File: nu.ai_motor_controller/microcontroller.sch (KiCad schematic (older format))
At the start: 2 parts

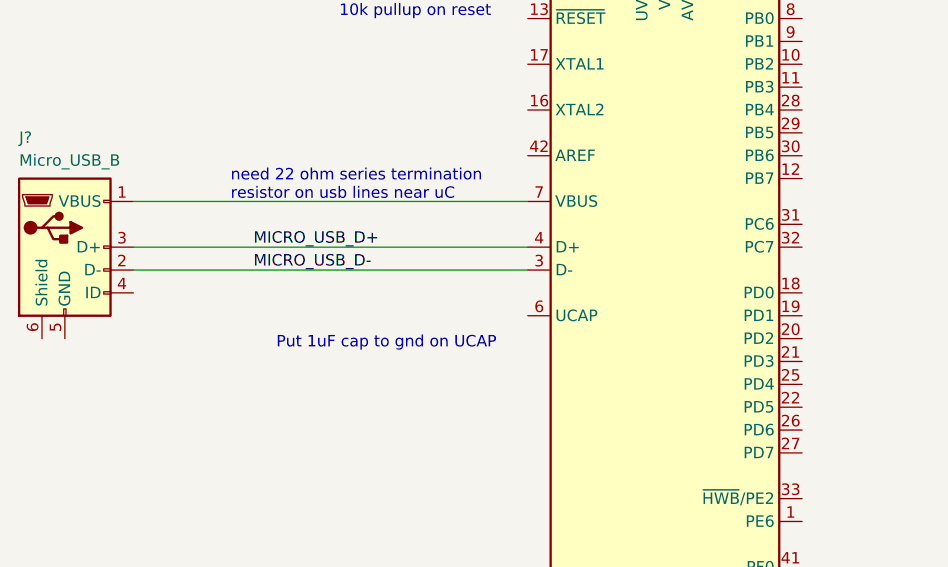
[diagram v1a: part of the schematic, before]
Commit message: Added termination resistors
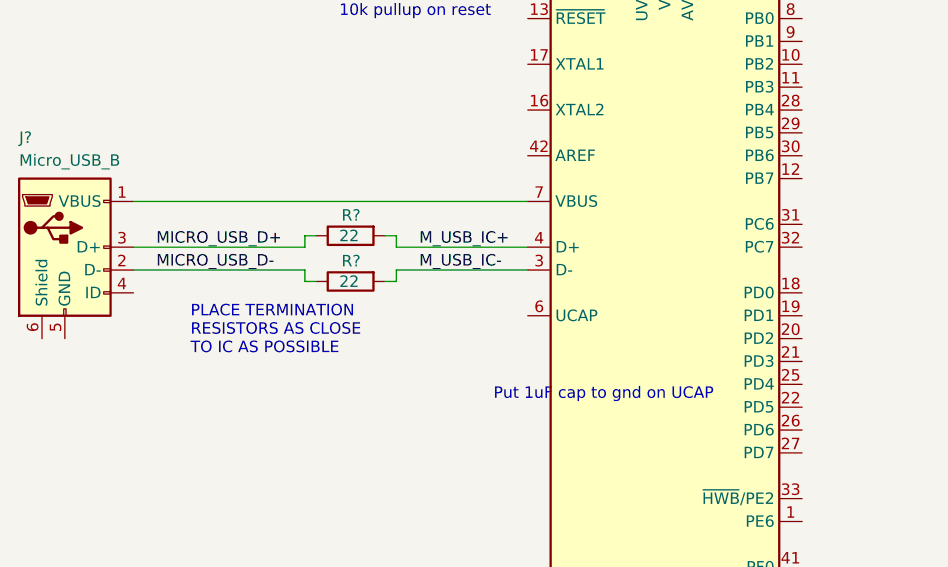
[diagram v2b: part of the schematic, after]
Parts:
- added R? (x2): RMCF0603FT22R0, 0603, symbol custom:RMCF0603FT22R0
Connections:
- net MICRO_USB_D+: now also R?.2; no longer U?.4 (D+)
- net MICRO_USB_D-: now also R?.2; no longer U?.3 (D-)
- new net M_USB_IC+: R?.1, U?.4 (D+)
- new net M_USB_IC-: R?.1, U?.3 (D-)
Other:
- note added: "PLACE TERMINATION\nRESISTORS AS CLOSE\nTO IC AS POSSIBLE"
- note removed: "need 22 ohm series termination\nresistor on usb lines near uC"
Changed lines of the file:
@@
 	1    0    0    -1
 $EndComp
-Wire Wire Line
-	3000 3225 4725 3225
-Wire Wire Line
-	4725 3325 3000 3325
-Text Label 3525 3225 0    50   ~ 0
+Text Label 3100 3225 0    50   ~ 0
 MICRO_USB_D+
-Text Label 3525 3325 0    50   ~ 0
+Text Label 3100 3325 0    50   ~ 0
 MICRO_USB_D-
-Text Notes 3425 3025 0    50   ~ 0
-need 22 ohm series termination\nresistor on usb lines near uC
+Text Notes 3250 3700 0    50   ~ 0
+PLACE TERMINATION\nRESISTORS AS CLOSE\nTO IC AS POSSIBLE
 Wire Wire Line
 	3000 3025 4725 3025
-Text Notes 3625 3675 0    50   ~ 0
+Text Notes 4575 3900 0    50   ~ 0
 Put 1uF cap to gnd on UCAP
 Text Notes 3900 2225 0    50   ~ 0
@@
 Text Notes 5475 1850 0    50   ~ 0
 Connect AVCC to VCC\nthrough a low pass filter
+$Comp
+L custom:RMCF0603FT22R0 R?
+U 1 1 5C4048F8
+P 3950 3375
+F 0 "R?" V 3890 3335 50  0000 L BNN
+F 1 "RMCF0603FT22R0" V 4075 3050 50  0001 L BNN
+F 2 "0603" V 4150 3275 50  0001 L BNN
+F 3 "~/datasheets/SEI-RMCF_RMCP.pdf" V 4250 3425 50  0001 C CNN
+F 4 "22" V 3980 3325 50  0000 L BNN "Resistance"
+	1    3950 3375
+	0    1    1    0
+$EndComp
+$Comp
+L custom:RMCF0603FT22R0 R?
+U 1 1 5C404A44
+P 3950 3175
+F 0 "R?" V 3890 3135 50  0000 L BNN
+F 1 "RMCF0603FT22R0" V 4075 2850 50  0001 L BNN
+F 2 "0603" V 4150 3075 50  0001 L BNN
+F 3 "~/datasheets/SEI-RMCF_RMCP.pdf" V 4250 3225 50  0001 C CNN
+F 4 "22" V 3980 3125 50  0000 L BNN "Resistance"
+	1    3950 3175
+	0    1    1    0
+$EndComp
+Wire Wire Line
+	4100 3175 4150 3175
+Wire Wire Line
+	4150 3175 4150 3225
+Wire Wire Line
+	4150 3225 4725 3225
+Wire Wire Line
+	4725 3325 4150 3325
+Wire Wire Line
+	4150 3325 4150 3375
+Wire Wire Line
+	4150 3375 4100 3375
+Wire Wire Line
+	3800 3375 3750 3375
+Wire Wire Line
+	3750 3325 3000 3325
+Wire Wire Line
+	3750 3325 3750 3375
+Wire Wire Line
+	3000 3225 3750 3225
+Wire Wire Line
+	3750 3225 3750 3175
+Wire Wire Line
+	3750 3175 3800 3175
+Text Label 4250 3225 0    50   ~ 0
+M_USB_IC+
+Text Label 4250 3325 0    50   ~ 0
+M_USB_IC-
 $EndSCHEMATC

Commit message: automated commit
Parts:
- added C?: CL10B105KA8NNNC, Capacitor_SMD:C_0603_1608Metric, symbol custom:CL10B105KA8NNNC
- added R?: CR0603-JW-103ELF, 0603, symbol custom:CR0603-JW-103ELF
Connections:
- net labels added: GND
- wire segments 13 -> 19
- no-connect marks 0 -> 1
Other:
- note added: "connect to power\n"
- note removed: "10k pullup on reset"
- note removed: "Put 1uF cap to gnd on UCAP"
- moved on the sheet: J?, R?, U?
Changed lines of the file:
@@
 L MCU_Microchip_ATmega:ATmega32U4-AU U?
 U 1 1 5C3ED06E
-P 5325 3725
-F 0 "U?" H 4825 5475 50  0000 L BNN
-F 1 "ATmega32U4-AU" H 5425 1975 50  0000 L TNN
-F 2 "Package_QFP:TQFP-44_10x10mm_P0.8mm" H 5325 3725 50  0001 C CIN
-F 3 "http://ww1.microchip.com/downloads/en/DeviceDoc/Atmel-7766-8-bit-AVR-ATmega16U4-32U4_Datasheet.pdf" H 5325 3725 50  0001 C CNN
-	1    5325 3725
+P 5350 3700
+F 0 "U?" H 4850 5450 50  0000 L BNN
+F 1 "ATmega32U4-AU" H 5450 1950 50  0000 L TNN
+F 2 "Package_QFP:TQFP-44_10x10mm_P0.8mm" H 5350 3700 50  0001 C CIN
+F 3 "http://ww1.microchip.com/downloads/en/DeviceDoc/Atmel-7766-8-bit-AVR-ATmega16U4-32U4_Datasheet.pdf" H 5350 3700 50  0001 C CNN
+	1    5350 3700
 	1    0    0    -1
 $EndComp
@@
 L custom:DX4R105JJCR1800 J?
 U 1 1 5C3ED2E2
-P 2700 3225
-F 0 "J?" H 2500 3675 50  0000 L BNN
-F 1 "DX4R105JJCR1800" H 2400 2425 50  0001 L BNN
-F 2 "" H 2850 3175 50  0001 C CNN
-F 3 "SJ113218.pdf" H 2850 3175 50  0001 L BNN
-F 4 "Micro_USB_B" H 2500 3575 50  0000 L BNN "Description"
-	1    2700 3225
+P 2000 3200
+F 0 "J?" H 1800 3650 50  0000 L BNN
+F 1 "DX4R105JJCR1800" H 1700 2400 50  0001 L BNN
+F 2 "" H 2150 3150 50  0001 C CNN
+F 3 "SJ113218.pdf" H 2150 3150 50  0001 L BNN
+F 4 "Micro_USB_B" H 1800 3550 50  0000 L BNN "Description"
+	1    2000 3200
 	1    0    0    -1
 $EndComp
-Text Label 3100 3225 0    50   ~ 0
+Text Label 3050 3200 0    50   ~ 0
 MICRO_USB_D+
-Text Label 3100 3325 0    50   ~ 0
+Text Label 3050 3300 0    50   ~ 0
 MICRO_USB_D-
-Text Notes 3250 3700 0    50   ~ 0
+Text Notes 3225 3675 0    50   ~ 0
 PLACE TERMINATION\nRESISTORS AS CLOSE\nTO IC AS POSSIBLE
 Wire Wire Line
-	3000 3025 4725 3025
-Text Notes 4575 3900 0    50   ~ 0
-Put 1uF cap to gnd on UCAP
-Text Notes 3900 2225 0    50   ~ 0
-10k pullup on reset
+	2300 3000 4750 3000
 Text Notes 5475 1850 0    50   ~ 0
 Connect AVCC to VCC\nthrough a low pass filter
@@
 L custom:RMCF0603FT22R0 R?
 U 1 1 5C4048F8
-P 3950 3375
-F 0 "R?" V 3890 3335 50  0000 L BNN
-F 1 "RMCF0603FT22R0" V 4075 3050 50  0001 L BNN
-F 2 "0603" V 4150 3275 50  0001 L BNN
-F 3 "~/datasheets/SEI-RMCF_RMCP.pdf" V 4250 3425 50  0001 C CNN
-F 4 "22" V 3980 3325 50  0000 L BNN "Resistance"
-	1    3950 3375
+P 3900 3350
+F 0 "R?" V 3840 3310 50  0000 L BNN
+F 1 "RMCF0603FT22R0" V 4025 3025 50  0001 L BNN
+F 2 "0603" V 4100 3250 50  0001 L BNN
+F 3 "~/datasheets/SEI-RMCF_RMCP.pdf" V 4200 3400 50  0001 C CNN
+F 4 "22" V 3930 3300 50  0000 L BNN "Resistance"
+	1    3900 3350
 	0    1    1    0
 $EndComp
@@
 L custom:RMCF0603FT22R0 R?
 U 1 1 5C404A44
-P 3950 3175
-F 0 "R?" V 3890 3135 50  0000 L BNN
-F 1 "RMCF0603FT22R0" V 4075 2850 50  0001 L BNN
-F 2 "0603" V 4150 3075 50  0001 L BNN
-F 3 "~/datasheets/SEI-RMCF_RMCP.pdf" V 4250 3225 50  0001 C CNN
-F 4 "22" V 3980 3125 50  0000 L BNN "Resistance"
-	1    3950 3175
+P 3900 3150
+F 0 "R?" V 3840 3110 50  0000 L BNN
+F 1 "RMCF0603FT22R0" V 4025 2825 50  0001 L BNN
+F 2 "0603" V 4100 3050 50  0001 L BNN
+F 3 "~/datasheets/SEI-RMCF_RMCP.pdf" V 4200 3200 50  0001 C CNN
+F 4 "22" V 3930 3100 50  0000 L BNN "Resistance"
+	1    3900 3150
 	0    1    1    0
 $EndComp
 Wire Wire Line
-	4100 3175 4150 3175
+	4050 3150 4100 3150
 Wire Wire Line
-	4150 3175 4150 3225
+	4100 3150 4100 3200
 Wire Wire Line
-	4150 3225 4725 3225
+	4100 3300 4100 3350
 Wire Wire Line
-	4725 3325 4150 3325
+	4100 3350 4050 3350
 Wire Wire Line
-	4150 3325 4150 3375
+	3750 3350 3700 3350
 Wire Wire Line
-	4150 3375 4100 3375
+	3700 3300 2300 3300
 Wire Wire Line
-	3800 3375 3750 3375
+	3700 3300 3700 3350
 Wire Wire Line
-	3750 3325 3000 3325
+	2300 3200 3700 3200
 Wire Wire Line
-	3750 3325 3750 3375
+	3700 3200 3700 3150
 Wire Wire Line
-	3000 3225 3750 3225
+	3700 3150 3750 3150
+Text Label 4200 3200 0    50   ~ 0
+M_USB_IC+
+Text Label 4200 3300 0    50   ~ 0
+M_USB_IC-
+$Comp
+L custom:CL10B105KA8NNNC C?
+U 1 1 5C414E9B
+P 4650 3750
+F 0 "C?" H 4800 3850 50  0000 L BNN
+F 1 "CL10B105KA8NNNC" H 3700 3300 50  0001 L BNN
+F 2 "Capacitor_SMD:C_0603_1608Metric" H 3700 3200 50  0001 L BNN
+F 3 "datasheets/CL10B105KA8NNNC.pdf" H 3700 3100 50  0001 L BNN
+F 4 "1uF" H 4800 3750 50  0000 L BNN "Capacitance"
+F 5 "25V" H 4800 3650 50  0000 L BNN "Rating"
+	1    4650 3750
+	-1   0    0    -1
+$EndComp
+$Comp
+L power:GND #PWR?
+U 1 1 5C414F68
+P 4650 3950
+F 0 "#PWR?" H 4650 3700 50  0001 C CNN
+F 1 "GND" H 4650 3800 50  0000 C CNN
+F 2 "" H 4650 3950 50  0001 C CNN
+F 3 "" H 4650 3950 50  0001 C CNN
+	1    4650 3950
+	1    0    0    -1
+$EndComp
 Wire Wire Line
-	3750 3225 3750 3175
+	4650 3950 4650 3900
 Wire Wire Line
-	3750 3175 3800 3175
-Text Label 4250 3225 0    50   ~ 0
-M_USB_IC+
-Text Label 4250 3325 0    50   ~ 0
-M_USB_IC-
+	4650 3600 4650 3500
+Wire Wire Line
+	4650 3500 4750 3500
+Wire Wire Line
+	4100 3300 4750 3300
+Wire Wire Line
+	4100 3200 4750 3200
+$Comp
+L custom:CR0603-JW-103ELF R?
+U 1 1 5C41A4AA
+P 4650 1950
+F 0 "R?" V 4590 1910 50  0000 L BNN
+F 1 "CR0603-JW-103ELF" V 4775 1625 50  0001 L BNN
+F 2 "0603" V 4850 1850 50  0001 L BNN
+F 3 "~/datasheets/chpreztr.pdf" V 4950 1500 50  0001 L BNN
+F 4 "10k" V 4680 1880 50  0000 L BNN "Resistance"
+	1    4650 1950
+	1    0    0    -1
+$EndComp
+Wire Wire Line
+	4650 2100 4650 2200
+Wire Wire Line
+	4650 2200 4750 2200
+Wire Wire Line
+	4650 1800 4650 1700
+Text Notes 4300 1600 0    50   ~ 0
+connect to power\n
+NoConn ~ 2300 3400
 $EndSCHEMATC

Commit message: automated commit
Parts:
- added L?: CIS10P300AC, 0603, symbol custom:CIS10P300AC
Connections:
- net labels added: +5V
- wire segments 19 -> 25
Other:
- note removed: "Connect AVCC to VCC\nthrough a low pass filter"
- note removed: "connect to power\n"
- moved on the sheet: R?
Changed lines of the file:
@@
 Wire Wire Line
 	2300 3000 4750 3000
-Text Notes 5475 1850 0    50   ~ 0
-Connect AVCC to VCC\nthrough a low pass filter
 $Comp
 L custom:RMCF0603FT22R0 R?
@@
 L custom:CR0603-JW-103ELF R?
 U 1 1 5C41A4AA
-P 4650 1950
-F 0 "R?" V 4590 1910 50  0000 L BNN
-F 1 "CR0603-JW-103ELF" V 4775 1625 50  0001 L BNN
-F 2 "0603" V 4850 1850 50  0001 L BNN
-F 3 "~/datasheets/chpreztr.pdf" V 4950 1500 50  0001 L BNN
-F 4 "10k" V 4680 1880 50  0000 L BNN "Resistance"
-	1    4650 1950
+P 4650 1750
+F 0 "R?" V 4590 1710 50  0000 L BNN
+F 1 "CR0603-JW-103ELF" V 4775 1425 50  0001 L BNN
+F 2 "0603" V 4850 1650 50  0001 L BNN
+F 3 "~/datasheets/chpreztr.pdf" V 4950 1300 50  0001 L BNN
+F 4 "10k" V 4680 1680 50  0000 L BNN "Resistance"
+	1    4650 1750
 	1    0    0    -1
 $EndComp
 Wire Wire Line
-	4650 2100 4650 2200
+	4650 1900 4650 2200
 Wire Wire Line
 	4650 2200 4750 2200
+NoConn ~ 2300 3400
+$Comp
+L custom:CIS10P300AC L?
+U 1 1 5C41689A
+P 5450 1700
+F 0 "L?" H 5550 1700 50  0000 L BNN
+F 1 "CIS10P300AC" H 5550 1400 50  0001 L BNN
+F 2 "0603" H 5550 1500 50  0001 L BNN
+F 3 "~/datasheets/CIS10P300AC.pdf" H 5550 1300 50  0001 L BNN
+F 4 "30@100MHz" H 5550 1600 50  0000 L BNN "Impedance"
+	1    5450 1700
+	1    0    0    -1
+$EndComp
 Wire Wire Line
-	4650 1800 4650 1700
-Text Notes 4300 1600 0    50   ~ 0
-connect to power\n
-NoConn ~ 2300 3400
+	5450 1900 5450 1850
+$Comp
+L power:+5V #PWR?
+U 1 1 5C416CDF
+P 5350 1450
+F 0 "#PWR?" H 5350 1300 50  0001 C CNN
+F 1 "+5V" H 5350 1590 50  0000 C CNN
+F 2 "" H 5350 1450 50  0001 C CNN
+F 3 "" H 5350 1450 50  0001 C CNN
+	1    5350 1450
+	1    0    0    -1
+$EndComp
+$Comp
+L power:+5V #PWR?
+U 1 1 5C416CFF
+P 4650 1450
+F 0 "#PWR?" H 4650 1300 50  0001 C CNN
+F 1 "+5V" H 4650 1590 50  0000 C CNN
+F 2 "" H 4650 1450 50  0001 C CNN
+F 3 "" H 4650 1450 50  0001 C CNN
+	1    4650 1450
+	1    0    0    -1
+$EndComp
+Wire Wire Line
+	4650 1450 4650 1600
+Wire Wire Line
+	5350 1450 5350 1500
+Wire Wire Line
+	5450 1550 5450 1500
+Wire Wire Line
+	5450 1500 5350 1500
+Connection ~ 5350 1500
+Wire Wire Line
+	5350 1500 5350 1900
+$Comp
+L power:GND #PWR?
+U 1 1 5C417D83
+P 5350 5600
+F 0 "#PWR?" H 5350 5350 50  0001 C CNN
+F 1 "GND" H 5350 5450 50  0000 C CNN
+F 2 "" H 5350 5600 50  0001 C CNN
+F 3 "" H 5350 5600 50  0001 C CNN
+	1    5350 5600
+	1    0    0    -1
+$EndComp
+Wire Wire Line
+	5350 5600 5350 5500
 $EndSCHEMATC

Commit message: automated commit
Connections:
- net +5V: now also U?.2 (UVCC)
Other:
- note added: "put .5A resettable fuse on vbus\n"
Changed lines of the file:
@@
 	4650 1450 4650 1600
 Wire Wire Line
-	5350 1450 5350 1500
-Wire Wire Line
-	5450 1550 5450 1500
-Wire Wire Line
 	5450 1500 5350 1500
-Connection ~ 5350 1500
-Wire Wire Line
-	5350 1500 5350 1900
 $Comp
 L power:GND #PWR?
@@
 Wire Wire Line
 	5350 5600 5350 5500
+Wire Wire Line
+	5250 1900 5250 1800
+Wire Wire Line
+	5250 1800 5350 1800
+Connection ~ 5350 1800
+Wire Wire Line
+	5350 1800 5350 1900
+Wire Wire Line
+	5350 1500 5350 1800
+Connection ~ 5350 1500
+Wire Wire Line
+	5350 1450 5350 1500
+Wire Wire Line
+	5450 1550 5450 1500
+Text Notes 2900 2950 0    50   ~ 0
+put .5A resettable fuse on vbus\n
 $EndSCHEMATC

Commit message: automated commit
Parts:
- added C?: CL10B104KO8NNNC, Capacitor_SMD:C_0603_1608Metric, symbol custom:CL10B104KO8NNNC
- added C?: CL10B105KA8NNNC, Capacitor_SMD:C_0603_1608Metric, symbol custom:CL10B105KA8NNNC
- added L?: CIS10P300AC, 0603, symbol custom:CIS10P300AC
- added R?: RC0603JR-071KL, 0603, symbol custom:RC0603JR-071KL
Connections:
- net labels added: M_USB_D+, M_USB_D-, UGND, VBUS
- net labels removed: MICRO_USB_D+, MICRO_USB_D-
- wire segments 28 -> 47
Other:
- note added: "use CM1293A-04SO on data lines"
- moved on the sheet: J?, R?
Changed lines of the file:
@@
 L custom:DX4R105JJCR1800 J?
 U 1 1 5C3ED2E2
-P 2000 3200
-F 0 "J?" H 1800 3650 50  0000 L BNN
-F 1 "DX4R105JJCR1800" H 1700 2400 50  0001 L BNN
-F 2 "" H 2150 3150 50  0001 C CNN
-F 3 "SJ113218.pdf" H 2150 3150 50  0001 L BNN
-F 4 "Micro_USB_B" H 1800 3550 50  0000 L BNN "Description"
-	1    2000 3200
-	1    0    0    -1
-$EndComp
-Text Label 3050 3200 0    50   ~ 0
-MICRO_USB_D+
-Text Label 3050 3300 0    50   ~ 0
-MICRO_USB_D-
-Text Notes 3225 3675 0    50   ~ 0
+P 1550 1975
+F 0 "J?" H 1350 2425 50  0000 L BNN
+F 1 "DX4R105JJCR1800" H 1250 1175 50  0001 L BNN
+F 2 "" H 1700 1925 50  0001 C CNN
+F 3 "SJ113218.pdf" H 1700 1925 50  0001 L BNN
+F 4 "Micro_USB_B" H 1350 2325 50  0000 L BNN "Description"
+	1    1550 1975
+	1    0    0    -1
+$EndComp
+Text Label 1875 1975 0    50   ~ 0
+M_USB_D+
+Text Label 1875 2075 0    50   ~ 0
+M_USB_D-
+Text Notes 2250 2425 0    50   ~ 0
 PLACE TERMINATION\nRESISTORS AS CLOSE\nTO IC AS POSSIBLE
-Wire Wire Line
-	2300 3000 4750 3000
 $Comp
 L custom:RMCF0603FT22R0 R?
 U 1 1 5C4048F8
-P 3900 3350
-F 0 "R?" V 3840 3310 50  0000 L BNN
-F 1 "RMCF0603FT22R0" V 4025 3025 50  0001 L BNN
-F 2 "0603" V 4100 3250 50  0001 L BNN
-F 3 "~/datasheets/SEI-RMCF_RMCP.pdf" V 4200 3400 50  0001 C CNN
-F 4 "22" V 3930 3300 50  0000 L BNN "Resistance"
-	1    3900 3350
+P 2525 2125
+F 0 "R?" V 2465 2085 50  0000 L BNN
+F 1 "RMCF0603FT22R0" V 2650 1800 50  0001 L BNN
+F 2 "0603" V 2725 2025 50  0001 L BNN
+F 3 "~/datasheets/SEI-RMCF_RMCP.pdf" V 2825 2175 50  0001 C CNN
+F 4 "22" V 2555 2075 50  0000 L BNN "Resistance"
+	1    2525 2125
 	0    1    1    0
 $EndComp
@@
 L custom:RMCF0603FT22R0 R?
 U 1 1 5C404A44
-P 3900 3150
-F 0 "R?" V 3840 3110 50  0000 L BNN
-F 1 "RMCF0603FT22R0" V 4025 2825 50  0001 L BNN
-F 2 "0603" V 4100 3050 50  0001 L BNN
-F 3 "~/datasheets/SEI-RMCF_RMCP.pdf" V 4200 3200 50  0001 C CNN
-F 4 "22" V 3930 3100 50  0000 L BNN "Resistance"
-	1    3900 3150
+P 2525 1925
+F 0 "R?" V 2465 1885 50  0000 L BNN
+F 1 "RMCF0603FT22R0" V 2650 1600 50  0001 L BNN
+F 2 "0603" V 2725 1825 50  0001 L BNN
+F 3 "~/datasheets/SEI-RMCF_RMCP.pdf" V 2825 1975 50  0001 C CNN
+F 4 "22" V 2555 1875 50  0000 L BNN "Resistance"
+	1    2525 1925
 	0    1    1    0
 $EndComp
 Wire Wire Line
-	4050 3150 4100 3150
-Wire Wire Line
-	4100 3150 4100 3200
-Wire Wire Line
-	4100 3300 4100 3350
-Wire Wire Line
-	4100 3350 4050 3350
-Wire Wire Line
-	3750 3350 3700 3350
-Wire Wire Line
-	3700 3300 2300 3300
-Wire Wire Line
-	3700 3300 3700 3350
-Wire Wire Line
-	2300 3200 3700 3200
-Wire Wire Line
-	3700 3200 3700 3150
-Wire Wire Line
-	3700 3150 3750 3150
-Text Label 4200 3200 0    50   ~ 0
+	2675 1925 2725 1925
+Wire Wire Line
+	2725 1925 2725 1975
+Wire Wire Line
+	2725 2075 2725 2125
+Wire Wire Line
+	2725 2125 2675 2125
+Wire Wire Line
+	2375 2125 2325 2125
+Wire Wire Line
+	2325 2075 1850 2075
+Wire Wire Line
+	2325 2075 2325 2125
+Wire Wire Line
+	1850 1975 2325 1975
+Wire Wire Line
+	2325 1975 2325 1925
+Wire Wire Line
+	2325 1925 2375 1925
+Text Label 4275 3200 0    50   ~ 0
 M_USB_IC+
-Text Label 4200 3300 0    50   ~ 0
+Text Label 4275 3300 0    50   ~ 0
 M_USB_IC-
 $Comp
@@
 U 1 1 5C414E9B
 P 4650 3750
-F 0 "C?" H 4800 3850 50  0000 L BNN
+F 0 "C?" H 4450 3800 50  0000 L BNN
 F 1 "CL10B105KA8NNNC" H 3700 3300 50  0001 L BNN
 F 2 "Capacitor_SMD:C_0603_1608Metric" H 3700 3200 50  0001 L BNN
 F 3 "datasheets/CL10B105KA8NNNC.pdf" H 3700 3100 50  0001 L BNN
-F 4 "1uF" H 4800 3750 50  0000 L BNN "Capacitance"
-F 5 "25V" H 4800 3650 50  0000 L BNN "Rating"
+F 4 "1uF" H 4400 3725 50  0000 L BNN "Capacitance"
+F 5 "25V" H 4400 3650 50  0000 L BNN "Rating"
 	1    4650 3750
-	-1   0    0    -1
+	1    0    0    -1
 $EndComp
 $Comp
@@
 Wire Wire Line
 	4650 3500 4750 3500
-Wire Wire Line
-	4100 3300 4750 3300
-Wire Wire Line
-	4100 3200 4750 3200
 $Comp
 L custom:CR0603-JW-103ELF R?
@@
 Wire Wire Line
 	4650 2200 4750 2200
-NoConn ~ 2300 3400
+NoConn ~ 1850 2175
 $Comp
 L custom:CIS10P300AC L?
@@
 L power:GND #PWR?
 U 1 1 5C417D83
-P 5350 5600
-F 0 "#PWR?" H 5350 5350 50  0001 C CNN
-F 1 "GND" H 5350 5450 50  0000 C CNN
-F 2 "" H 5350 5600 50  0001 C CNN
-F 3 "" H 5350 5600 50  0001 C CNN
-	1    5350 5600
-	1    0    0    -1
-$EndComp
-Wire Wire Line
-	5350 5600 5350 5500
+P 5350 6175
+F 0 "#PWR?" H 5350 5925 50  0001 C CNN
+F 1 "GND" H 5350 6025 50  0000 C CNN
+F 2 "" H 5350 6175 50  0001 C CNN
+F 3 "" H 5350 6175 50  0001 C CNN
+	1    5350 6175
+	1    0    0    -1
+$EndComp
+Wire Wire Line
+	5350 6175 5350 6125
 Wire Wire Line
 	5250 1900 5250 1800
@@
 Wire Wire Line
 	5450 1550 5450 1500
-Text Notes 2900 2950 0    50   ~ 0
+Text Notes 1950 1725 0    50   ~ 0
 put .5A resettable fuse on vbus\n
+$Comp
+L custom:CIS10P300AC L?
+U 1 1 5C41773B
+P 5250 5925
+F 0 "L?" H 5450 5925 50  0000 L BNN
+F 1 "CIS10P300AC" H 5350 5625 50  0001 L BNN
+F 2 "0603" H 5350 5725 50  0001 L BNN
+F 3 "~/datasheets/CIS10P300AC.pdf" H 5350 5525 50  0001 L BNN
+F 4 "30@100MHz" H 5350 5825 50  0000 L BNN "Impedance"
+	1    5250 5925
+	-1   0    0    -1
+$EndComp
+Wire Wire Line
+	5250 6075 5250 6125
+Wire Wire Line
+	5250 6125 5350 6125
+Connection ~ 5350 6125
+Wire Wire Line
+	5350 6125 5350 5500
+Wire Wire Line
+	5250 5775 5250 5500
+Text Label 5250 5550 3    50   ~ 0
+UGND
+Text Label 1650 2425 0    50   ~ 0
+UGND
+Wire Wire Line
+	1550 2375 1550 2425
+Wire Wire Line
+	1550 2425 1850 2425
+$Comp
+L custom:CL10B105KA8NNNC C?
+U 1 1 5C41A0FF
+P 1225 2700
+F 0 "C?" H 1375 2800 50  0000 L BNN
+F 1 "CL10B105KA8NNNC" H 275 2250 50  0001 L BNN
+F 2 "Capacitor_SMD:C_0603_1608Metric" H 275 2150 50  0001 L BNN
+F 3 "datasheets/CL10B105KA8NNNC.pdf" H 275 2050 50  0001 L BNN
+F 4 "1uF" H 1375 2700 50  0000 L BNN "Capacitance"
+F 5 "25V" H 1375 2600 50  0000 L BNN "Rating"
+	1    1225 2700
+	-1   0    0    -1
+$EndComp
+$Comp
+L custom:RC0603JR-071KL R?
+U 1 1 5C41A493
+P 1450 2675
+F 0 "R?" V 1375 2625 50  0000 L BNN
+F 1 "RC0603JR-071KL" H 1525 2600 50  0001 L BNN
+F 2 "0603" H 1525 2675 50  0001 L BNN
+F 3 "~/datasheets/PYu-RC_Group_51_RoHS_L_10.pdf" H 1390 2685 50  0001 C CNN
+F 4 "1k" V 1475 2625 50  0000 L BNN "Resistance"
+	1    1450 2675
+	-1   0    0    -1
+$EndComp
+$Comp
+L power:GND #PWR?
+U 1 1 5C41A5DB
+P 1450 2975
+F 0 "#PWR?" H 1450 2725 50  0001 C CNN
+F 1 "GND" H 1450 2825 50  0000 C CNN
+F 2 "" H 1450 2975 50  0001 C CNN
+F 3 "" H 1450 2975 50  0001 C CNN
+	1    1450 2975
+	1    0    0    -1
+$EndComp
+Wire Wire Line
+	1450 2975 1450 2900
+Wire Wire Line
+	1225 2850 1225 2900
+Wire Wire Line
+	1225 2900 1450 2900
+Connection ~ 1450 2900
+Wire Wire Line
+	1450 2900 1450 2825
+Wire Wire Line
+	1225 2550 1225 2450
+Wire Wire Line
+	1225 2450 1450 2450
+Wire Wire Line
+	1450 2450 1450 2375
+Wire Wire Line
+	1450 2450 1450 2525
+Connection ~ 1450 2450
+Text Notes 2125 2850 0    50   ~ 0
+use CM1293A-04SO on data lines
+$Comp
+L custom:CL10B104KO8NNNC C?
+U 1 1 5C4180AD
+P 4200 3750
+F 0 "C?" H 3975 3800 50  0000 L BNN
+F 1 "CL10B104KO8NNNC" H 3250 3300 50  0001 L BNN
+F 2 "Capacitor_SMD:C_0603_1608Metric" H 3250 3200 50  0001 L BNN
+F 3 "datasheets/CL10B104KO8NNNC.pdf" H 3250 3100 50  0001 L BNN
+F 4 "0.1uF" H 3875 3725 50  0000 L BNN "Capacitance"
+F 5 "16V" H 3925 3650 50  0000 L BNN "Rating"
+	1    4200 3750
+	1    0    0    -1
+$EndComp
+Wire Wire Line
+	4200 3600 4200 2800
+Wire Wire Line
+	4200 2800 4750 2800
+$Comp
+L power:GND #PWR?
+U 1 1 5C418D5C
+P 4200 3950
+F 0 "#PWR?" H 4200 3700 50  0001 C CNN
+F 1 "GND" H 4200 3800 50  0000 C CNN
+F 2 "" H 4200 3950 50  0001 C CNN
+F 3 "" H 4200 3950 50  0001 C CNN
+	1    4200 3950
+	1    0    0    -1
+$EndComp
+Wire Wire Line
+	4200 3950 4200 3900
+Text Label 4475 3000 0    50   ~ 0
+VBUS
+Wire Wire Line
+	4475 3000 4750 3000
+Wire Wire Line
+	4275 3300 4750 3300
+Wire Wire Line
+	4750 3200 4275 3200
+Wire Wire Line
+	2725 1975 3100 1975
+Wire Wire Line
+	2725 2075 3100 2075
+Text Label 2750 1975 0    50   ~ 0
+M_USB_IC+
+Text Label 2750 2075 0    50   ~ 0
+M_USB_IC-
 $EndSCHEMATC
